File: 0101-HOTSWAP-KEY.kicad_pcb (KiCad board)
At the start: 2 copper layers, 24.6 x 19.6 mm, 5 parts, among them J1 Conn_01x04, SW1 SW_Push

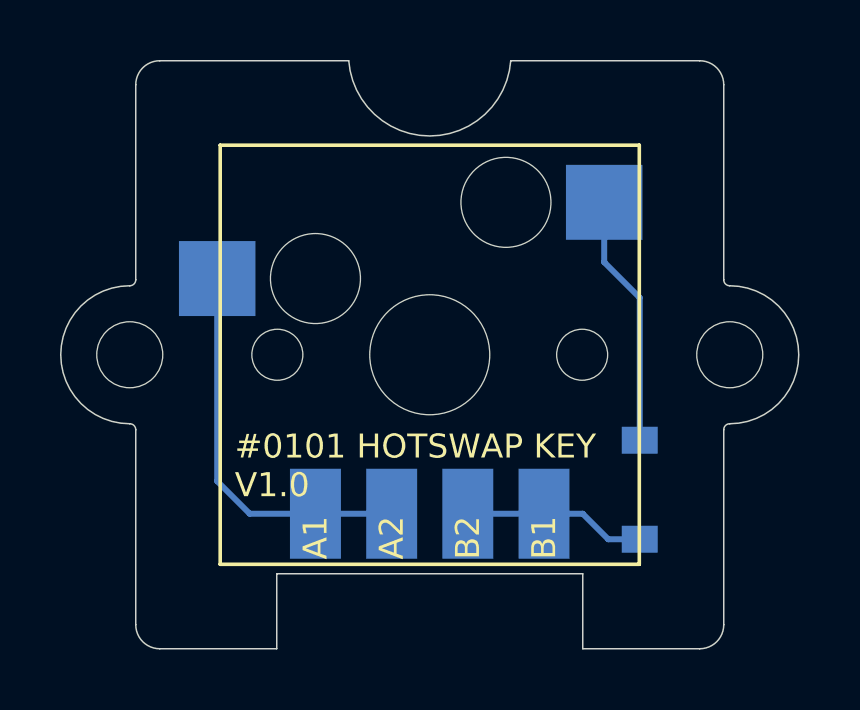
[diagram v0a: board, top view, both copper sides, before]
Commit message: Migrate to KiCad 6
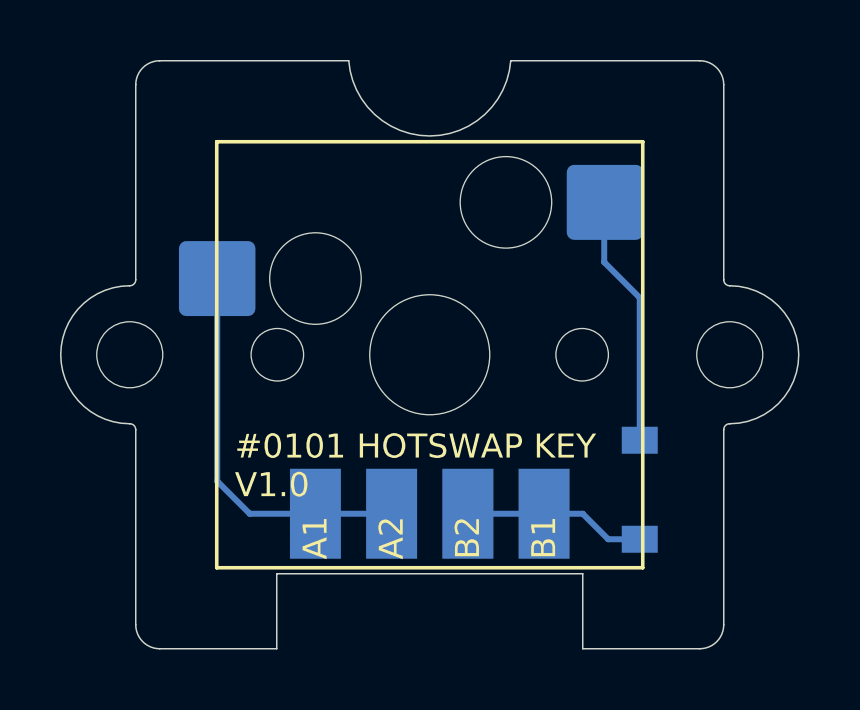
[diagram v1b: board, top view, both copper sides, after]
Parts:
- SW1: footprint JLC-SMT:KAILH_CPG151101S11 -> Switch_Keyboard_Hotswap_Kailh:SW_Hotswap_Kailh_MX_1.00u
- moved SW1 5.68 mm to (110.0, 110.0)
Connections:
- SW1 pad 1: Net-(D1-Pad1) -> /KEY_B_IN
- SW1 pad 2: /KEY_B_IN -> Net-(D1-Pad1)
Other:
- net class Default removed
- net class RF removed
- net class VCC removed

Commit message: Use kibuzzard silks
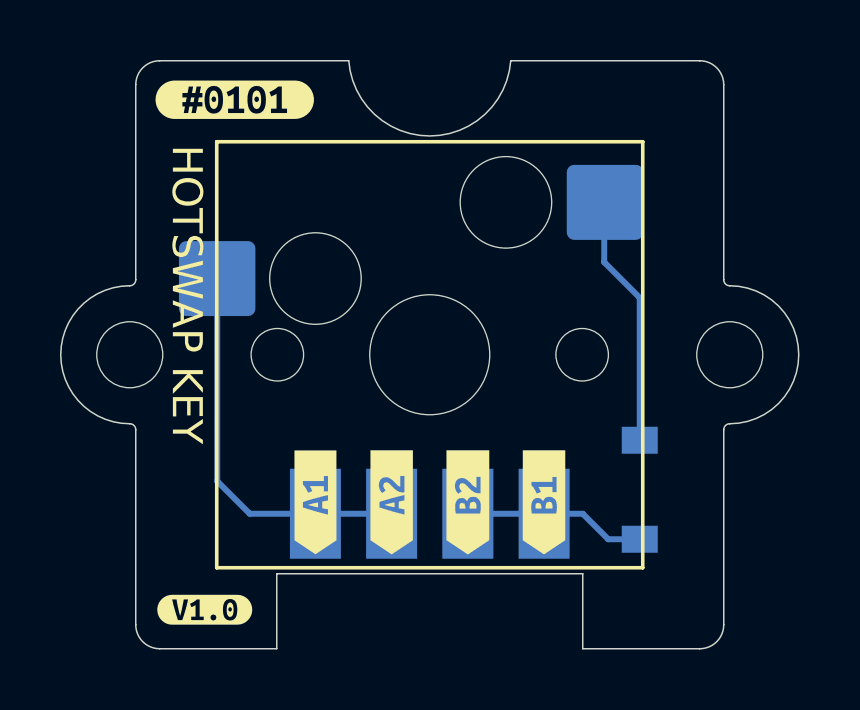
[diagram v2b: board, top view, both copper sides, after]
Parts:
- added kibuzzard-631DE0D4: G***, kibuzzard-631DE0D4, F.Cu at (106.2, 114.9)
- added kibuzzard-631DE0DB: G***, kibuzzard-631DE0DB, F.Cu at (108.7, 114.9)
- added kibuzzard-631DE0E9: G***, kibuzzard-631DE0E9, F.Cu at (111.3, 114.9)
- added kibuzzard-631DE0FD: G***, kibuzzard-631DE0FD, F.Cu at (113.8, 114.9)
- added kibuzzard-631DE163: G***, kibuzzard-631DE163, F.Cu at (103.5, 101.5)
- added kibuzzard-631DE1A7: G***, kibuzzard-631DE1A7, F.Cu at (102.5, 118.5)
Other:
- board text added: "HOTSWAP KEY"
- board text removed: "#0101 HOTSWAP KEY V1.0"
- board text removed: "A1"
- board text removed: "A2"
- board text removed: "B1"
- board text removed: "B2"
